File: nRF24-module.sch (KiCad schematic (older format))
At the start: 29 parts, among them P1 CONN_02X04, U1 STM32F302C8T, U2 SN65HVD256, U3 MCP1703, X1 16MHz 10ppm

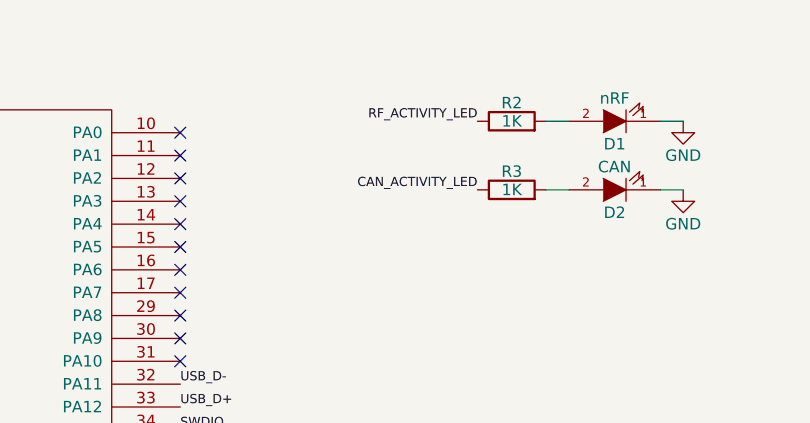
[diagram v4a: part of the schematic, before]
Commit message: Connect RX TX LEDs
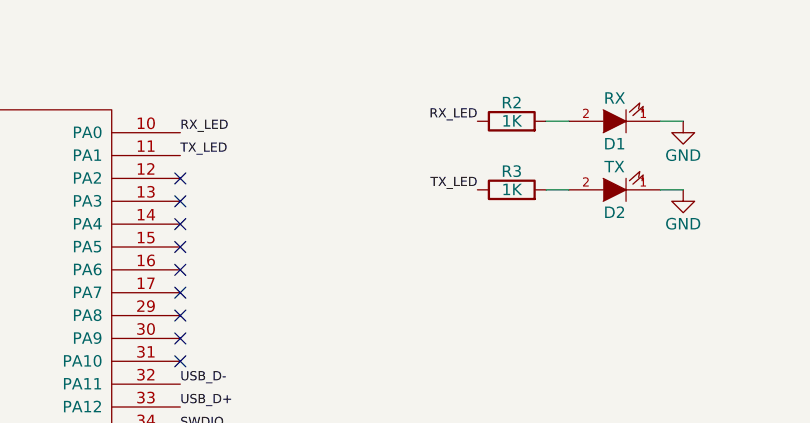
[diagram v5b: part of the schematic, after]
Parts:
- D1: value nRF -> RX
- D2: value CAN -> TX
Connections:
- net CAN_ACTIVITY_LED is gone; now on net TX_LED: R3.1
- net RF_ACTIVITY_LED is gone; now on net RX_LED: R2.1
- net RX_LED: now reaches U1.10 (PA0)
- net TX_LED: now reaches U1.11 (PA1)
- no-connect marks 24 -> 22
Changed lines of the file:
@@
 P 5500 1350
 F 0 "D1" H 5500 1450 50  0000 C CNN
-F 1 "nRF" H 5500 1250 50  0000 C CNN
+F 1 "RX" H 5500 1250 50  0000 C CNN
 F 2 "_std:_0603" H 5500 1350 60  0001 C CNN
 F 3 "" H 5500 1350 60  0000 C CNN
@@
 $EndComp
 Text Label 4900 1350 2    40   ~ 0
-RF_ACTIVITY_LED
+RX_LED
 $Comp
 L LED D2
@@
 P 5500 1650
 F 0 "D2" H 5500 1750 50  0000 C CNN
-F 1 "CAN" H 5500 1550 50  0000 C CNN
+F 1 "TX" H 5500 1550 50  0000 C CNN
 F 2 "_std:_0603" H 5500 1650 60  0001 C CNN
 F 3 "" H 5500 1650 60  0000 C CNN
@@
 $EndComp
 Text Label 4900 1650 2    40   ~ 0
-CAN_ACTIVITY_LED
+TX_LED
 NoConn ~ 3600 3300
 NoConn ~ 3600 3200
@@
 	1    0    0    -1
 $EndComp
-NoConn ~ 3600 1500
 NoConn ~ 3600 1600
 NoConn ~ 3600 2900
@@
 	1    0    0    -1
 $EndComp
-NoConn ~ 3600 1400
 $Comp
 L MCP1703 U3
@@
 Text Label 5450 3450 0    40   ~ 0
 SPI2_SCK
+Text Label 3600 1500 0    40   ~ 0
+TX_LED
+Text Label 3600 1400 0    40   ~ 0
+RX_LED
 $EndSCHEMATC

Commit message: Start with PCB component placement
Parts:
- CONN2: footprint _connectors:_Micro-USB-AB-receptacle-SMT -> _connectors:_Micro-USB-AB-receptacle-SMT-th
- U3: footprint (none) -> _std:_SOT23-3
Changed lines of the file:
@@
 F 0 "CONN2" H 10150 3900 60  0000 C CNN
 F 1 "MICRO_USB" H 10200 3100 60  0000 C CNN
-F 2 "_connectors:_Micro-USB-AB-receptacle-SMT" H 10150 3500 60  0001 C CNN
+F 2 "_connectors:_Micro-USB-AB-receptacle-SMT-th" H 10150 3500 60  0001 C CNN
 F 3 "" H 10150 3500 60  0000 C CNN
 	1    10150 3500
@@
 F 0 "U3" H 9650 1800 60  0000 C CNN
 F 1 "MCP1703" H 9350 1800 60  0000 C CNN
-F 2 "" H 9300 2050 60  0000 C CNN
+F 2 "_std:_SOT23-3" H 9300 2050 60  0001 C CNN
 F 3 "" H 9300 2050 60  0000 C CNN
 	1    9400 1600

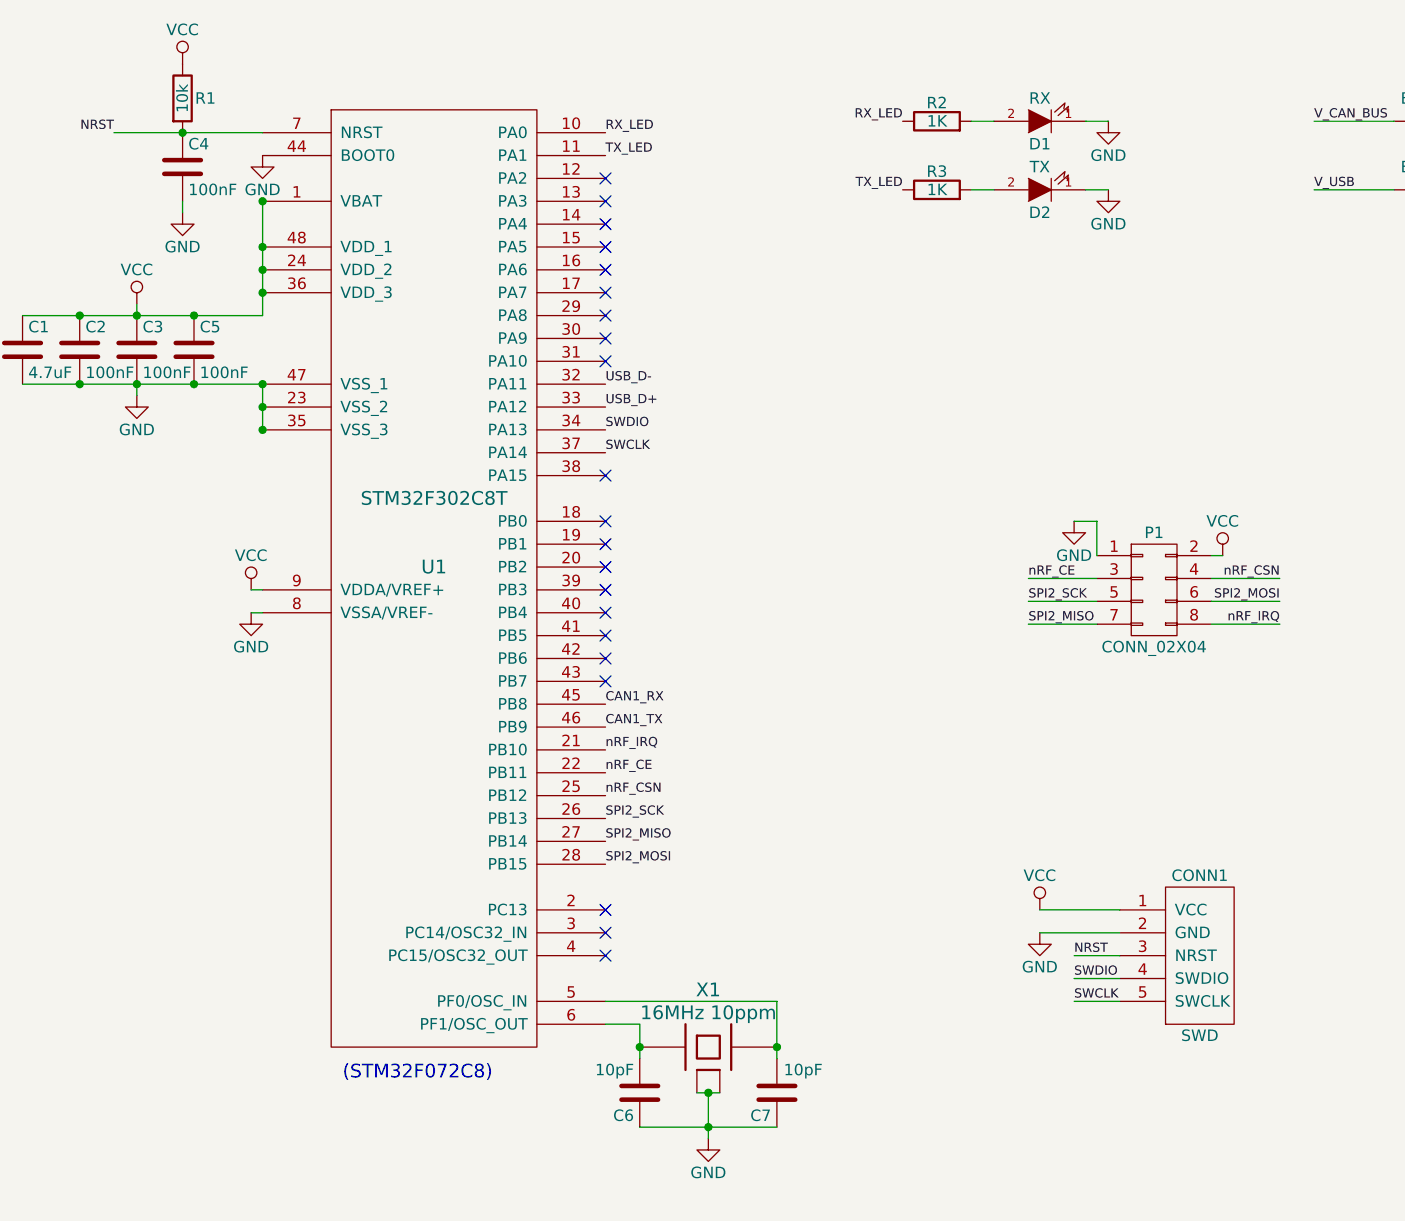
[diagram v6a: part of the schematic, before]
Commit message: Routing, change pins, add debug UART
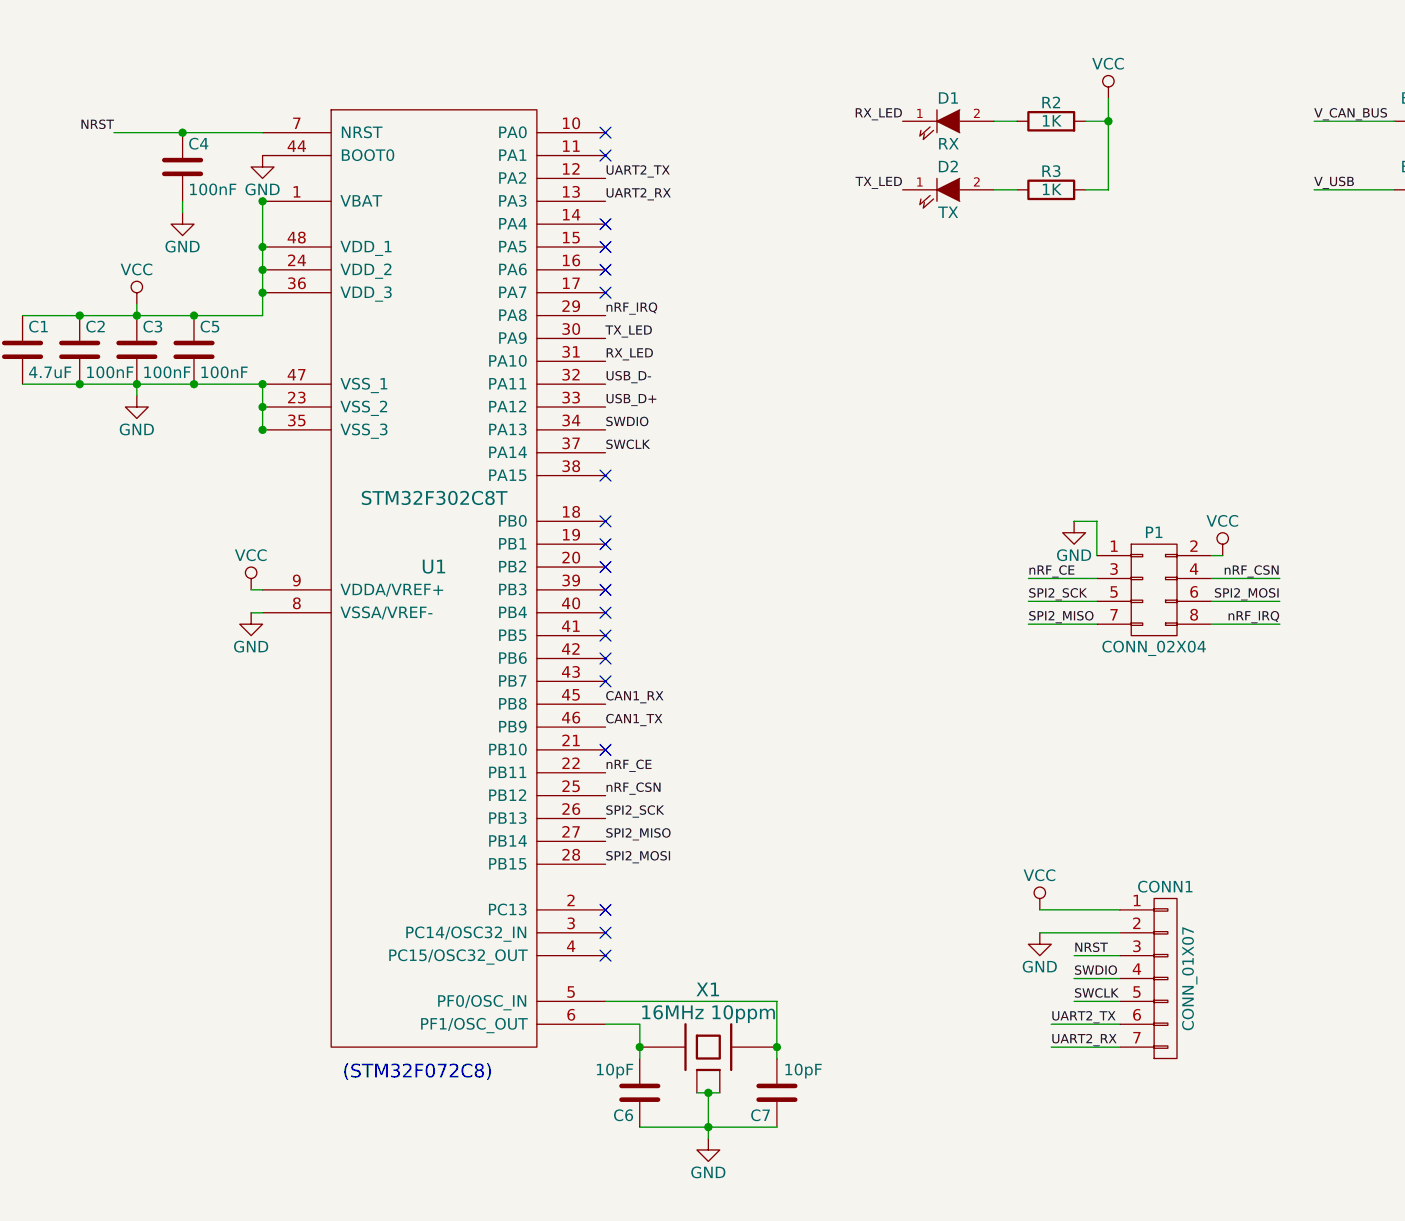
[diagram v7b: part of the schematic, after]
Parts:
- removed CONN1: SWD, _connectors:_Pin2mm_5z, symbol SWD
- removed R1: 10k, _std:_0603, symbol R
- added CONN1: CONN_01X07, Connectors_Molex:Connector_Molex_PicoBlade_53047-0710, symbol CONN_01X07
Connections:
- net GND: now also CONN1.2 (P2); no longer D1.1 (K), D2.1 (K)
- net NRST: now also CONN1.3 (P3)
- net RX_LED: now also D1.1 (K), U1.31 (PA10); no longer R2.1, U1.10 (PA0)
- net SWCLK: now also CONN1.5 (P5)
- net SWDIO: now also CONN1.4 (P4)
- net TX_LED: now also D2.1 (K), U1.30 (PA9); no longer R3.1, U1.11 (PA1)
- net VCC: now also R2.2, R3.2, CONN1.1 (P1)
- net nRF_IRQ: now also U1.29 (PA8); no longer U1.21 (PB10)
- net at D2.2 (A): now also R3.1; no longer R3.2
- net at D1.2 (A): now also R2.1; no longer R2.2
- net UART2_TX: now reaches U1.12 (PA2)
- net UART2_TX: now also CONN1.6 (P6)
- net UART2_RX: now reaches U1.13 (PA3)
- net UART2_RX: now also CONN1.7 (P7)
- no-connect marks 22 -> 20
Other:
- moved on the sheet: D1, D2, R2, R3

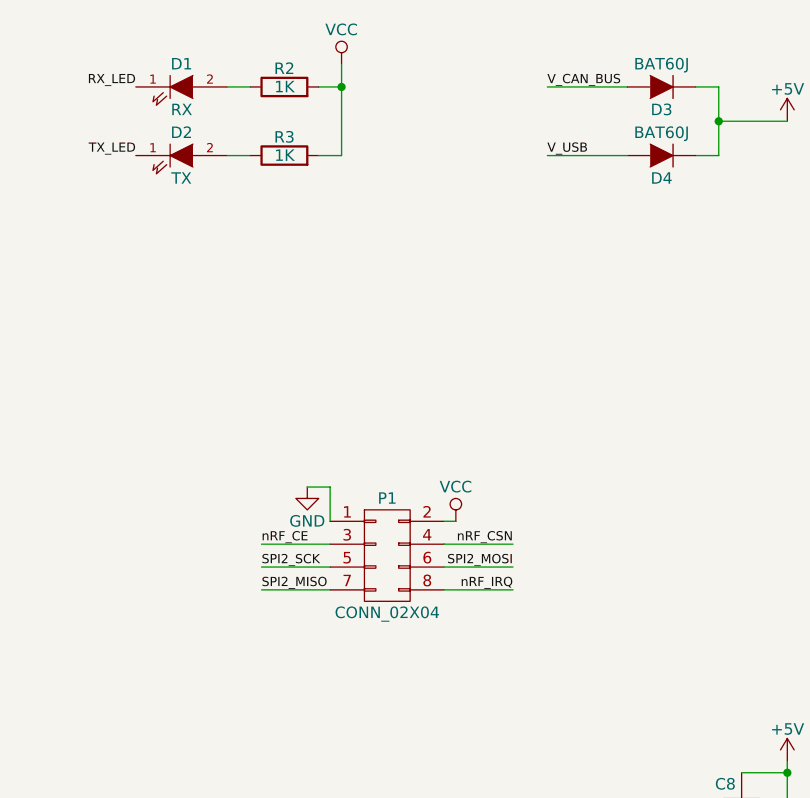
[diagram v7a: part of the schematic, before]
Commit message: Routing almost finished, add capacitor to nRF24 VCC
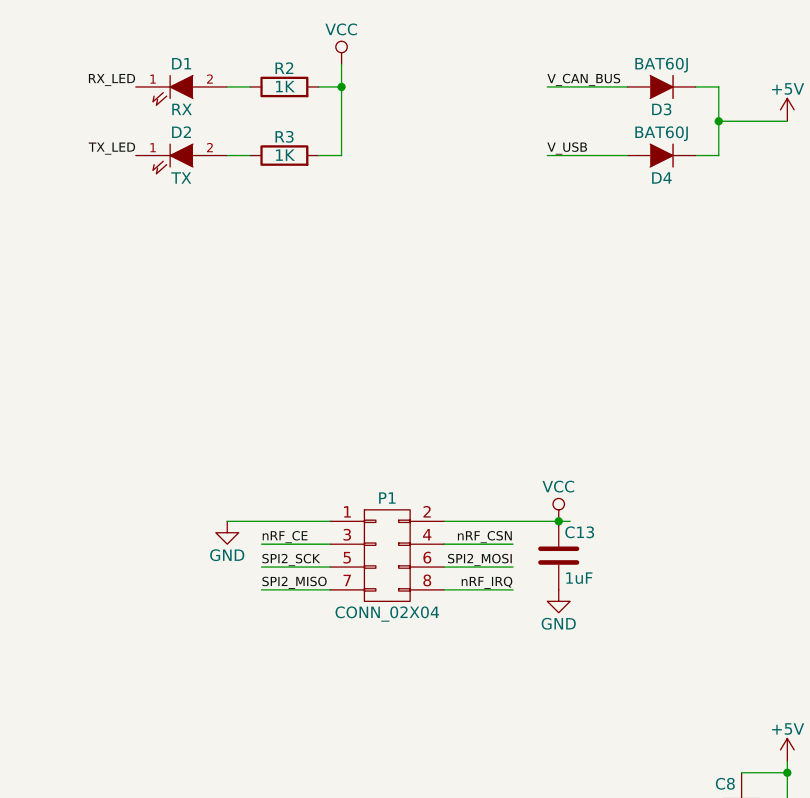
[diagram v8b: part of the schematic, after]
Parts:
- added C13: 1uF, _std:_0603, symbol C
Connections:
- net GND: now also C13.2
- net VCC: now also C13.1
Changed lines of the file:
@@
 L GND #PWR019
 U 1 1 563A8B10
-P 5650 3100
-F 0 "#PWR019" H 5650 2850 50  0001 C CNN
-F 1 "GND" H 5650 2950 50  0000 C CNN
-F 2 "" H 5650 3100 60  0000 C CNN
-F 3 "" H 5650 3100 60  0000 C CNN
-	1    5650 3100
+P 5300 3250
+F 0 "#PWR019" H 5300 3000 50  0001 C CNN
+F 1 "GND" H 5300 3100 50  0000 C CNN
+F 2 "" H 5300 3250 60  0000 C CNN
+F 3 "" H 5300 3250 60  0000 C CNN
+	1    5300 3250
 	1    0    0    -1
 $EndComp
@@
 L VCC #PWR020
 U 1 1 563A8C1C
-P 6300 3250
-F 0 "#PWR020" H 6300 3100 50  0001 C CNN
-F 1 "VCC" H 6300 3400 50  0000 C CNN
-F 2 "" H 6300 3250 60  0000 C CNN
-F 3 "" H 6300 3250 60  0000 C CNN
-	1    6300 3250
+P 6750 3250
+F 0 "#PWR020" H 6750 3100 50  0001 C CNN
+F 1 "VCC" H 6750 3400 50  0000 C CNN
+F 2 "" H 6750 3250 60  0000 C CNN
+F 3 "" H 6750 3250 60  0000 C CNN
+	1    6750 3250
 	1    0    0    -1
 $EndComp
@@
 	7450 1500 7750 1500
 Wire Wire Line
-	5650 3100 5750 3100
-Wire Wire Line
-	5750 3100 5750 3250
-Wire Wire Line
-	6250 3250 6300 3250
+	5300 3250 5750 3250
+Wire Wire Line
+	6250 3250 6800 3250
 Wire Wire Line
 	5450 3350 5750 3350
@@
 	7750 5150 7750 5150
 Wire Wire Line
-	5700 1650 5800 1650
+	5800 1650 5700 1650
 Wire Wire Line
 	5700 1350 5800 1350
@@
 $EndComp
 Wire Wire Line
-	5800 1650 5800 1250
+	5800 1250 5800 1650
 Connection ~ 5800 1350
 Wire Wire Line
@@
 Wire Wire Line
 	5400 1650 5300 1650
+$Comp
+L C C13
+U 1 1 56E76711
+P 6750 3400
+F 0 "C13" H 6775 3500 50  0000 L CNN
+F 1 "1uF" H 6775 3300 50  0000 L CNN
+F 2 "_std:_0603" H 6788 3250 30  0001 C CNN
+F 3 "" H 6750 3400 60  0000 C CNN
+	1    6750 3400
+	1    0    0    -1
+$EndComp
+Connection ~ 6750 3250
+$Comp
+L GND #PWR027
+U 1 1 56E76C2F
+P 6750 3550
+F 0 "#PWR027" H 6750 3300 50  0001 C CNN
+F 1 "GND" H 6750 3400 50  0000 C CNN
+F 2 "" H 6750 3550 50  0000 C CNN
+F 3 "" H 6750 3550 50  0000 C CNN
+	1    6750 3550
+	1    0    0    -1
+$EndComp
 $EndSCHEMATC
